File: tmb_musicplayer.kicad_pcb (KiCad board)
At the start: 2 copper layers, 99.1 x 95.3 mm, 192 parts, among them J2 RC522_Header, J3 Screw_Terminal_1x02, P1 SWD, P2 VolDown, P3 Prev, P4 Play, P5 Next, P6 VolUp, P7 CONN_02X10, Q1 BSS138, U1 VS1053, U2 STM32F407VGTx, U3 LD3985M18R, U4 LM22676QMRX-5.0, U5 LD3985M33R, U6 LD3985M33R, U7 LINEOUT, Y1 12.288 Mhz, Y2 8MHz

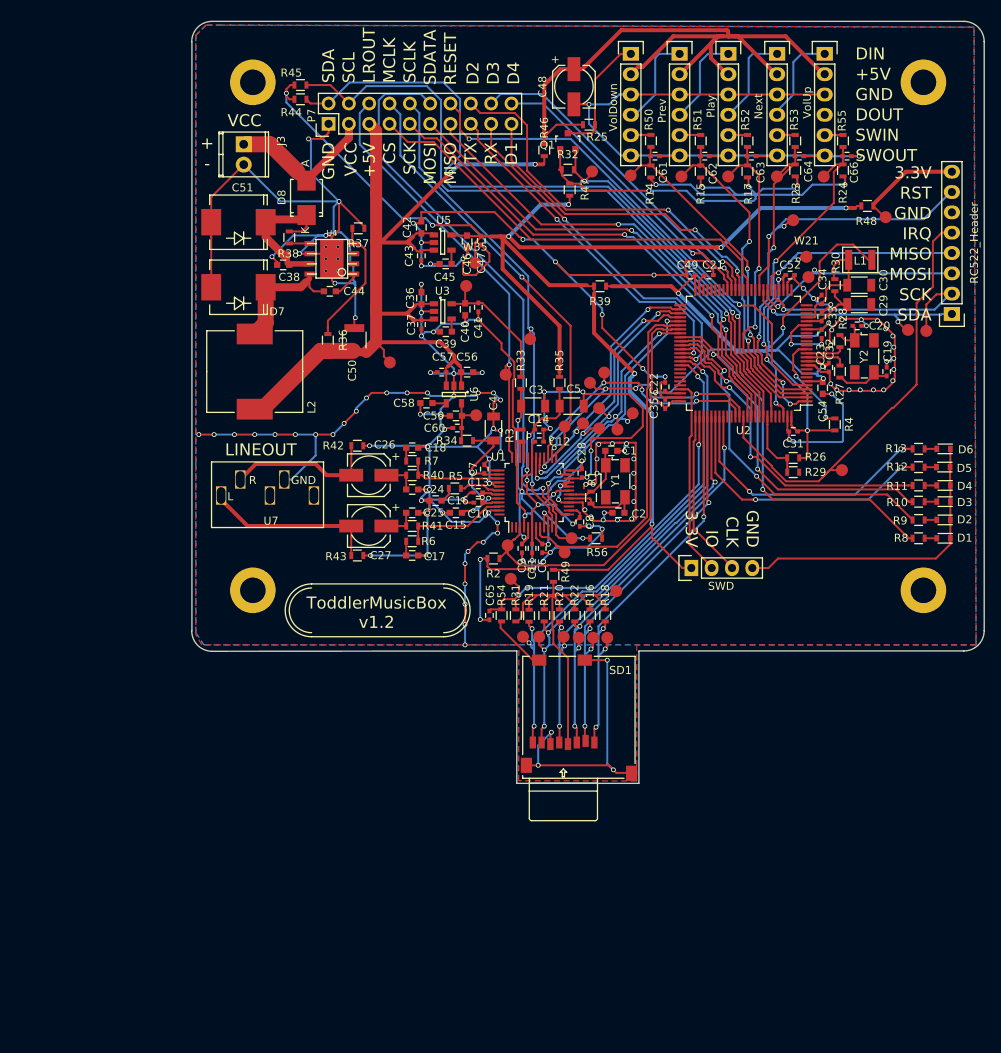
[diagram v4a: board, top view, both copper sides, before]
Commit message: Remove 3. LDO some improvements
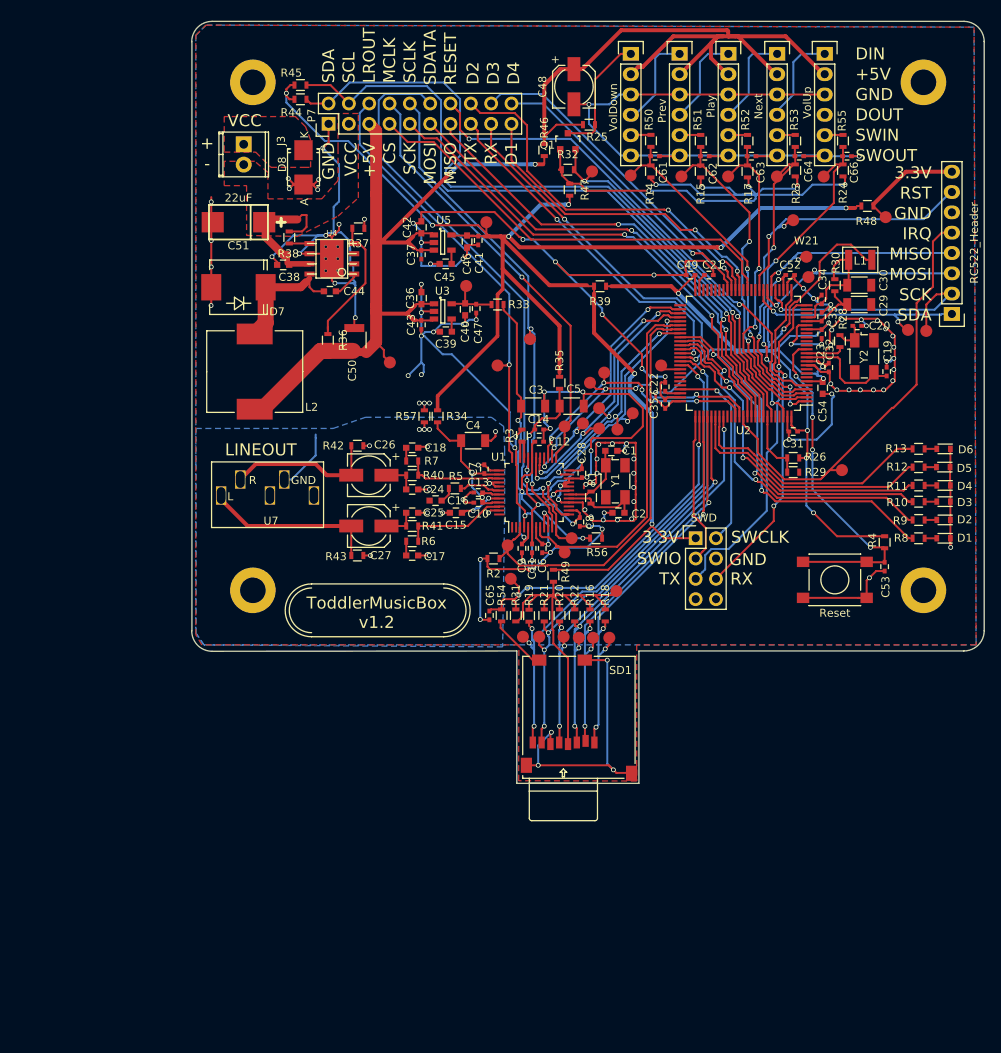
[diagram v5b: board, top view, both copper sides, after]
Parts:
- removed C56, C59: 1uF, Capacitors_SMD:C_0603
- removed C57, C60: 100nF, Capacitors_SMD:C_0402
- removed C58: 10nF, Capacitors_SMD:C_0603
- removed P1: SWD, Pin_Headers:Pin_Header_Straight_1x04
- removed R27: 0, Resistors_SMD:R_0603
- removed U6: LD3985M33R, TO_SOT_Packages_SMD:SOT-23-5
- removed W38: 3V3A, Measurement_Points:Measurement_Point_Round-SMD-Pad_Small
- added C53: 100nF, Capacitors_SMD:C_0402, F.Cu at (152.6, 119.0)
- added J1: SWD, Pin_Headers:Pin_Header_Straight_2x04, F.Cu at (129.0, 115.4)
- added R57: 0, Resistors_SMD:R_0603, F.Cu at (95.1, 100.2)
- added SW1: Reset, Buttons_Switches_SMD:SW_SPST_PTS645, F.Cu at (146.4, 120.6)
- added W39: MCO1, Measurement_Points:Measurement_Point_Round-SMD-Pad_Small, F.Cu at (124.7, 93.8)
- C1, C2: value 33pF -> 15pF
- C19, C20: value 20pF -> 15pF
- C26, C27: value 75uF -> 10uF
- C51: footprint Diodes_SMD:SMC_Standard -> jfi:SM2917_POL
- R4: value 100k -> 10k
- W22: value 3v3 -> 3V3
- W37: value 3V3A -> 5V
- moved R4 16.0 mm to (152.6, 115.9), turned to 90 degrees
- moved R33 10.2 mm to (104.2, 86.2), turned to 180 degrees
- moved C37 8.73 mm to (94.7, 80.0)
- moved C43 8.64 mm to (94.7, 88.7)
- moved C47 8.53 mm to (101.6, 86.7)
- moved C41 8.35 mm to (101.8, 78.2)
- moved W35 5.27 mm to (102.8, 75.9)
- moved R34 4.78 mm to (96.8, 100.2), turned to 90 degrees
- moved D8 3.83 mm to (80.0, 69.0), turned to 270 degrees
- moved C4 2.96 mm to (101.2, 103.2), turned to 0 degrees
- moved W13 1.53 mm to (104.2, 93.8)
- moved W25 0.25 mm to (118.2, 127.9)
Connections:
- net Net-(R4-Pad1) renamed /Main/NRST
- C10 pad 2: GND -> GNDA
- C13 pad 2: GND -> GNDA
- C15 pad 2: GND -> GNDA
- C16 pad 1: GND -> GNDA
- C17 pad 2: GND -> GNDA
- C18 pad 1: GND -> GNDA
- C24 pad 2: GND -> GNDA
- C25 pad 2: GND -> GNDA
- C38 pad 1: Net-(C38-Pad1) -> VCC
- C4 pad 2: GND -> GNDA
- C41 pad 1: +1V8 -> +3V3
- C47 pad 1: +3V3 -> +1V8
- C51 pad 1: Net-(C38-Pad1) -> VCC
- C7 pad 2: GND -> GNDA
- D8 pad 1: Net-(C38-Pad1) -> Net-(D8-Pad1)
- D8 pad 2: VCC -> GND
- J3 pad 1: VCC -> Net-(D8-Pad1)
- J3 pad 2: GND -> VCC
- R34 pad 2: +3.3VA -> +3V3
- R38 pad 1: Net-(C38-Pad1) -> VCC
- R42 pad 1: GND -> GNDA
- R43 pad 1: GND -> GNDA
- U1 pad 37: GND -> GNDA
- U1 pad 40: GND -> GNDA
- U1 pad 41: GND -> GNDA
- U1 pad 47: GND -> GNDA
- U2 pad 12: Net-(R27-Pad1) -> Net-(C19-Pad1)
- U2 pad 25: /Main/PA2 -> /PA2
- U2 pad 26: /Main/PA3 -> /PA3
- U4 pad 7: Net-(C38-Pad1) -> VCC
- U7 pad 3: GND -> GNDA
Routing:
- net GND: track 799.8 -> 582.6 mm, vias 138 -> 107
- net /PA2: track 0.00 -> 41.9 mm, vias 0 -> 1
- net /PA3: track 0.00 -> 41.5 mm, vias 0 -> 2
- net GNDA: track 0.00 -> 31.3 mm, vias 0 -> 15
- net /Main/NRST: track 12.7 -> 43.8 mm, vias 2 -> 4
- net Net-(C38-Pad1): track 20.8 -> 0.00 mm
- net +3V3: track 196.0 -> 215.6 mm
- net +5V: track 119.9 -> 102.1 mm
- net VDD: track 142.5 -> 156.8 mm, vias 8 -> 10
- net CVDD: track 53.4 -> 65.1 mm
- net +1V8: track 17.3 -> 7.30 mm
- net Net-(C19-Pad1): track 7.02 -> 13.8 mm
- net +3.3VA: track 6.72 -> 0.00 mm
- net Net-(R27-Pad1): track 5.05 -> 0.00 mm
- net /PD0: track 34.8 -> 31.6 mm, vias 2 -> 0
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- added copper zone on B.Cu, net GNDA
- added copper zone on F.Cu, net Net-(D8-Pad1)
- added copper zone on F.Cu, net VCC
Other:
- board text added: "SWCLK"
- board text added: "SWIO"
- board text removed: "CLK"
- board text removed: "IO"

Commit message: some minor improvements
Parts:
- added R27: NA, Resistors_SMD:R_0603, F.Cu at (80.5, 116.3)
- added R58: NA, Resistors_SMD:R_0603, F.Cu at (80.7, 106.0)
- added R59: NA, Resistors_SMD:R_0603, F.Cu at (76.8, 116.3)
- added R60: NA, Resistors_SMD:R_0603, F.Cu at (76.7, 106.0)
- added RV1: POT_TRIM, jfi:Potentiometer_WirePads_Small, F.Cu at (82.3, 118.6)
- added RV2: POT_TRIM, jfi:Potentiometer_WirePads_Small, F.Cu at (77.3, 103.7)
- SW1: value Reset -> SW_Push
- moved U7 1.14 mm to (68.5, 110.3)
- moved C26 0.46 mm to (88.4, 107.9)
- moved C27 0.46 mm to (88.4, 114.3)
- moved R42 0.46 mm to (87.0, 104.2)
- moved R43 0.46 mm to (87.0, 117.9)
- moved C18 0.46 mm to (93.8, 104.5)
- moved C24 0.46 mm to (93.8, 109.7)
- moved C25 0.46 mm to (93.8, 112.6)
- moved R40 0.46 mm to (93.8, 107.9)
- moved R41 0.46 mm to (93.8, 114.3)
- moved R6 0.46 mm to (93.8, 116.2)
- moved R7 0.46 mm to (93.8, 106.1)
- moved C17 0.36 mm to (93.8, 117.8)
- moved C16 0.28 mm to (96.4, 111.0)
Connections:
- U7 pad 1: Net-(C27-Pad2) -> Net-(R27-Pad1)
- U7 pad 2: Net-(C26-Pad2) -> Net-(R58-Pad2)
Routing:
- net Net-(R27-Pad1): track 0.00 -> 18.0 mm
- net Net-(R58-Pad2): track 0.00 -> 14.7 mm
- net Net-(C27-Pad2): track 21.8 -> 11.9 mm
- net Net-(C26-Pad2): track 18.9 -> 11.5 mm
- net GNDA: track 31.3 -> 29.6 mm, vias 15 -> 18
- net Net-(C25-Pad1): track 4.12 -> 4.62 mm

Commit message: Version 1.2
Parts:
- C1, C2: footprint Capacitors_SMD:C_0603 -> Capacitors_SMD:C_0402
- C26, C27: footprint Capacitors_SMD:c_elec_5x5.7 -> Capacitors_SMD:c_elec_4x5.7
- C48: value 75uF -> 10uF; footprint Capacitors_SMD:c_elec_5x5.7 -> Capacitors_SMD:c_elec_4x5.7
- L1: value 10uH -> FCM1608KF-601T03
- R27, R58: value NA -> 0
- RV1, RV2: value POT_TRIM -> 10k; footprint jfi:Potentiometer_WirePads_Small -> Potentiometers:Potentiometer_WirePads_Small
- moved W37 7.76 mm to (91.2, 85.7)
- moved R36 6.02 mm to (87.5, 86.6)
- moved C50 1.37 mm to (87.6, 90.1), turned to 180 degrees
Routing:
- net Net-(R36-Pad1): track 16.5 -> 10.3 mm
- net GND: track 582.6 -> 587.6 mm, vias 107 -> 108
- net +5V: track 102.1 -> 106.7 mm
- net /PD6: track 33.9 -> 32.8 mm
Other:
- board text removed: "Left"

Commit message: Fixed footprint of L1
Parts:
- L1: footprint MF_Passives:MF_Passives-L1210 -> Resistors_SMD:R_0603
- RV1, RV2: footprint Potentiometers:Potentiometer_WirePads_Small -> jfi:Potentiometer_WirePads_Small_nosilk
- moved L1 1.59 mm to (148.2, 79.8), turned to 270 degrees
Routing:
- net VDD: track 157.1 -> 152.8 mm
- net /Main/VDDA: track 15.3 -> 14.4 mm
- net GND: vias 108 -> 109
